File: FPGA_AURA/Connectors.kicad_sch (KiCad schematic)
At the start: 1 part, among them J1 ST5-40-1.00-L-D-P-TR

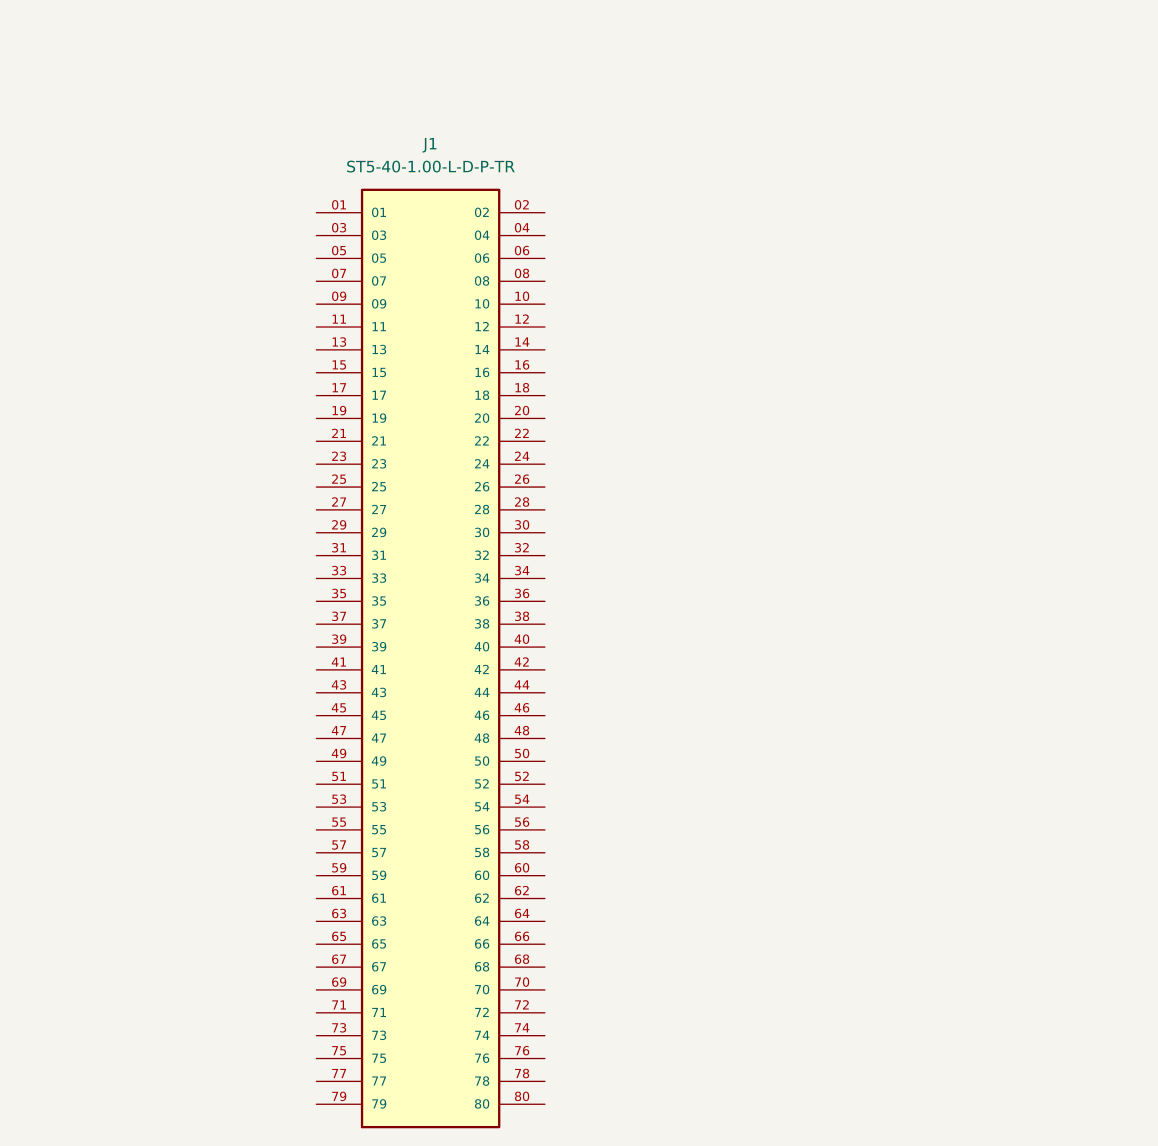
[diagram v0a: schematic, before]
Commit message: All DDR3 traces broken out, next stage is delay matching, and verifying break out through Vivado
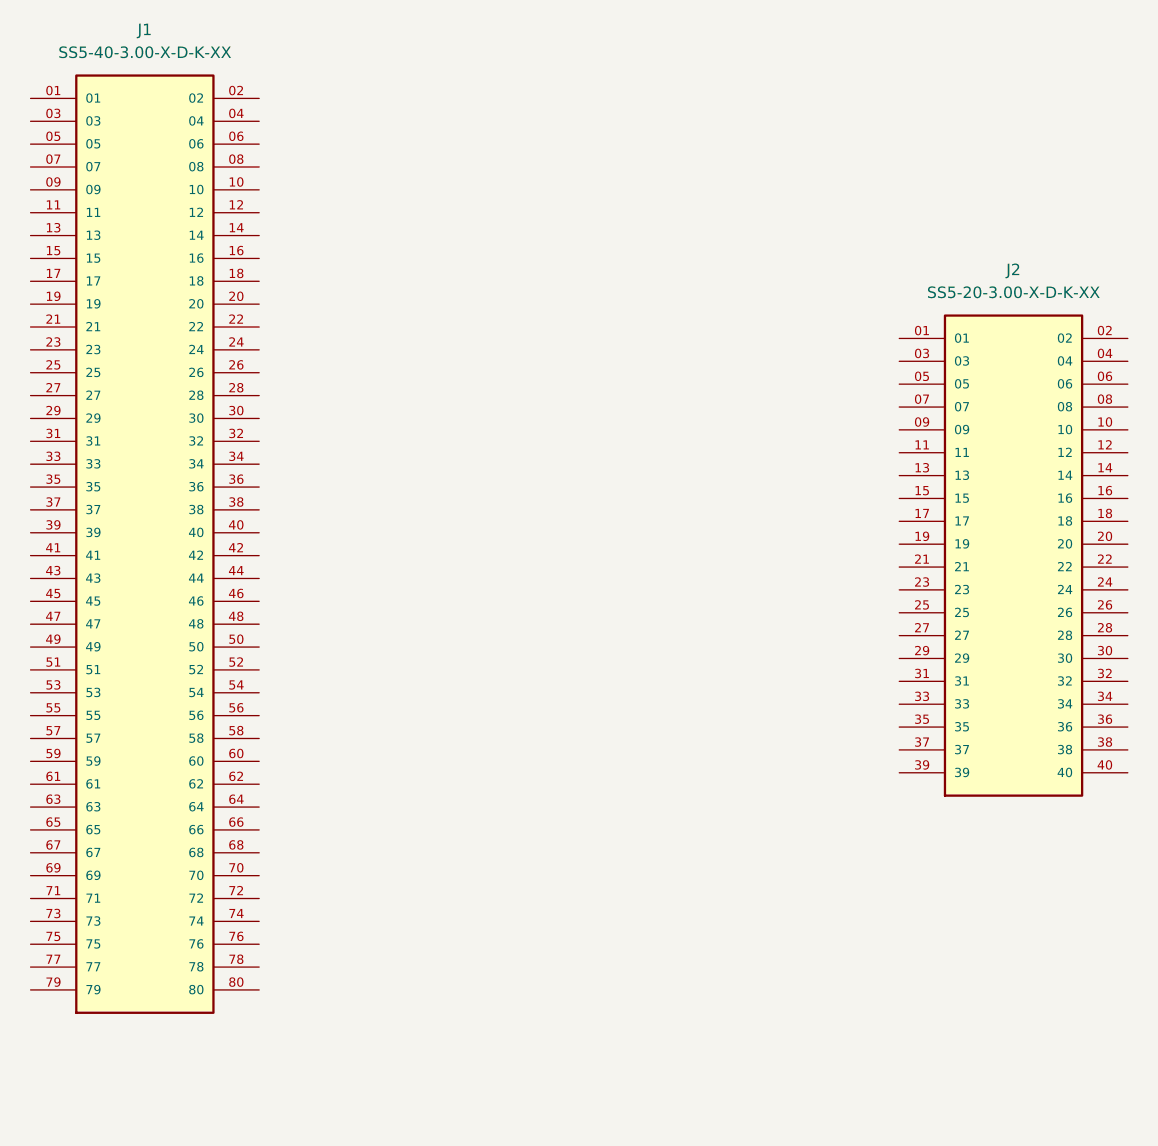
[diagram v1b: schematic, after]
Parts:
- removed J1: ST5-40-1.00-L-D-P-TR, ST5-40-1.00-L-D-P-TR:ST5-40-1.00-L-D-P-TR, symbol ST5-40-1.00-L-D-P-TR:ST5-40-1.00-L-D-P-TR
- added J1: SS5-40-3.00-X-D-K-XX, SS5-40-3.00-X-D-K-XX:SAMTEC_SS5-40-3.00-X-D-K-XX, symbol SS5-40-3.00-X-D-K-XX:SS5-40-3.00-X-D-K-XX
- added J2: SS5-20-3.00-X-D-K-XX, SS5-20-3.00-X-D-K-XX:SAMTEC_SS5-20-3.00-X-D-K-XX, symbol SS5-20-3.00-X-D-K-XX:SS5-20-3.00-X-D-K-XX

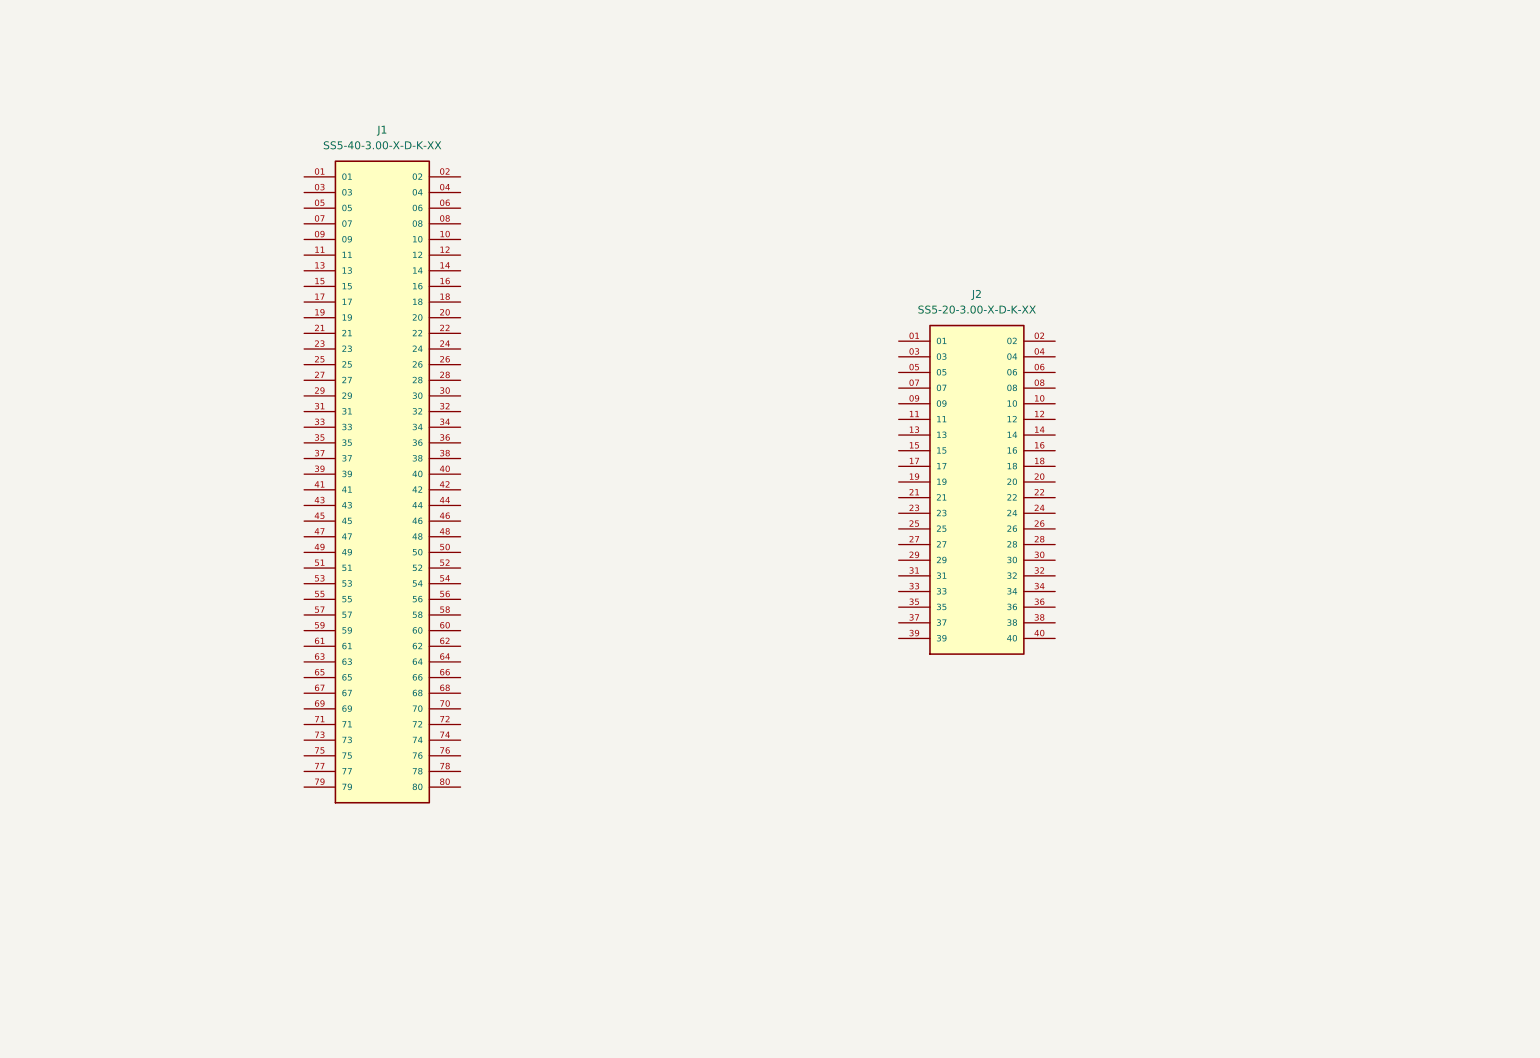
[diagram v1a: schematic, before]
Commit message: Connector pinnout defined loosly. Next is schematic clean-up followed by routing.
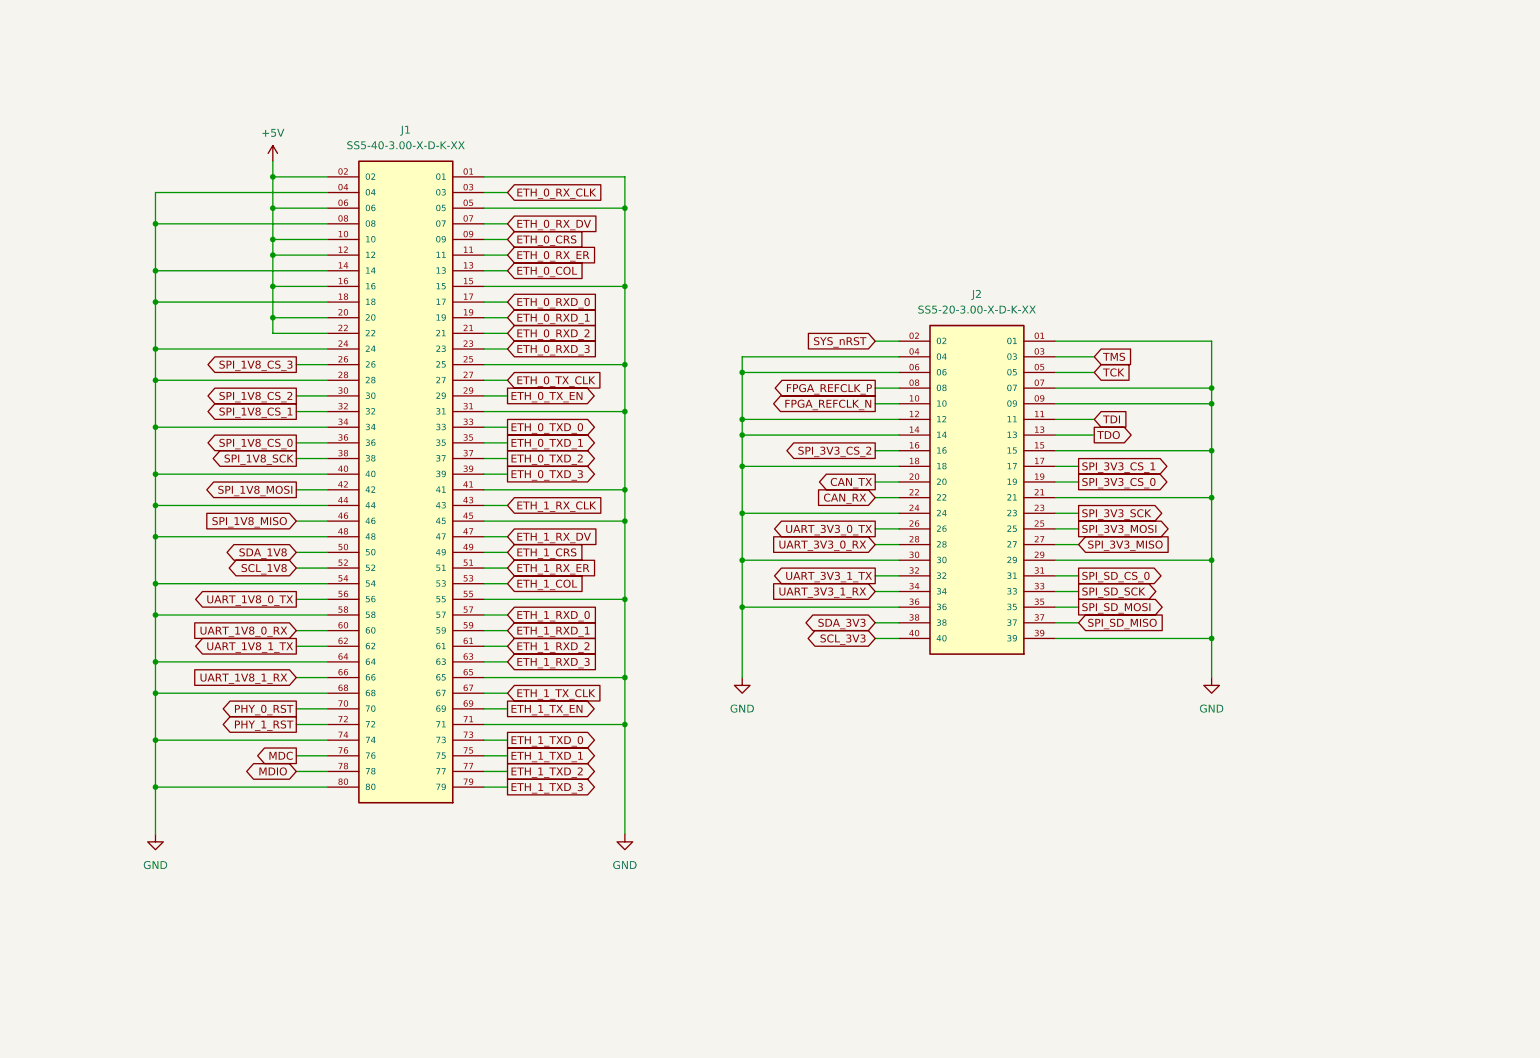
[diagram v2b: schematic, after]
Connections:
- net GND: now reaches J1.01
- net GND: now also J1.04, J1.05, J1.08, J1.14, J1.15, J1.18, J1.24, J1.25, J1.28, J1.31, J1.34, J1.40, J1.41, J1.44, J1.45, J1.48, J1.54, J1.55, J1.58, J1.64, J1.65, J1.68, J1.71, J1.74, J1.80, J2.01, J2.04, J2.06, J2.07, J2.09, J2.12, J2.14, J2.15, J2.18, J2.21, J2.24, J2.29, J2.30, J2.36, J2.39
- net +5V: now reaches J1.02
- net +5V: now also J1.06, J1.10, J1.12, J1.16, J1.20, J1.22
- net ETH_0_RX_CLK: now reaches J1.03
- net ETH_0_RX_DV: now reaches J1.07
- net ETH_0_CRS: now reaches J1.09
- net ETH_0_RX_ER: now reaches J1.11
- net ETH_0_COL: now reaches J1.13
- net ETH_0_RXD_0: now reaches J1.17
- net ETH_0_RXD_1: now reaches J1.19
- net ETH_0_RXD_2: now reaches J1.21
- net ETH_0_RXD_3: now reaches J1.23
- net SPI_1V8_CS_3: now reaches J1.26
- net ETH_0_TX_CLK: now reaches J1.27
- net ETH_0_TX_EN: now reaches J1.29
- net SPI_1V8_CS_2: now reaches J1.30
- net SPI_1V8_CS_1: now reaches J1.32
- net ETH_0_TXD_0: now reaches J1.33
- net ETH_0_TXD_1: now reaches J1.35
- net SPI_1V8_CS_0: now reaches J1.36
- net ETH_0_TXD_2: now reaches J1.37
- net SPI_1V8_SCK: now reaches J1.38
- net ETH_0_TXD_3: now reaches J1.39
- net SPI_1V8_MOSI: now reaches J1.42
- net ETH_1_RX_CLK: now reaches J1.43
- net SPI_1V8_MISO: now reaches J1.46
- net ETH_1_RX_DV: now reaches J1.47
- net ETH_1_CRS: now reaches J1.49
- net SDA_1V8: now reaches J1.50
- net ETH_1_RX_ER: now reaches J1.51
- net SCL_1V8: now reaches J1.52
- net ETH_1_COL: now reaches J1.53
- net UART_1V8_0_TX: now reaches J1.56
- net ETH_1_RXD_0: now reaches J1.57
- net ETH_1_RXD_1: now reaches J1.59
- net UART_1V8_0_RX: now reaches J1.60
- net ETH_1_RXD_2: now reaches J1.61
- net UART_1V8_1_TX: now reaches J1.62
- net ETH_1_RXD_3: now reaches J1.63
- net UART_1V8_1_RX: now reaches J1.66
- net ETH_1_TX_CLK: now reaches J1.67
- net ETH_1_TX_EN: now reaches J1.69
- net PHY_0_RST: now reaches J1.70
- net PHY_1_RST: now reaches J1.72
- net ETH_1_TXD_0: now reaches J1.73
- net ETH_1_TXD_1: now reaches J1.75
- net MDC: now reaches J1.76
- net ETH_1_TXD_2: now reaches J1.77
- net MDIO: now reaches J1.78
- net ETH_1_TXD_3: now reaches J1.79
- net SYS_nRST: now reaches J2.02
- net TMS: now reaches J2.03
- net TCK: now reaches J2.05
- net FPGA_REFCLK_P: now reaches J2.08
- net FPGA_REFCLK_N: now reaches J2.10
- net TDI: now reaches J2.11
- net TDO: now reaches J2.13
- net SPI_3V3_CS_2: now reaches J2.16
- net SPI_3V3_CS_1: now reaches J2.17
- net SPI_3V3_CS_0: now reaches J2.19
- net CAN_TX: now reaches J2.20
- net CAN_RX: now reaches J2.22
- net SPI_3V3_SCK: now reaches J2.23
- net SPI_3V3_MOSI: now reaches J2.25
- net UART_3V3_0_TX: now reaches J2.26
- net SPI_3V3_MISO: now reaches J2.27
- net UART_3V3_0_RX: now reaches J2.28
- net SPI_SD_CS_0: now reaches J2.31
- net UART_3V3_1_TX: now reaches J2.32
- net SPI_SD_SCK: now reaches J2.33
- net UART_3V3_1_RX: now reaches J2.34
- net SPI_SD_MOSI: now reaches J2.35
- net SPI_SD_MISO: now reaches J2.37
- net SDA_3V3: now reaches J2.38
- net SCL_3V3: now reaches J2.40
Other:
- moved on the sheet: J1
